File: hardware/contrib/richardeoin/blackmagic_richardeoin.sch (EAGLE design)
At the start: 5 parts, among them Q2 IRLML5103

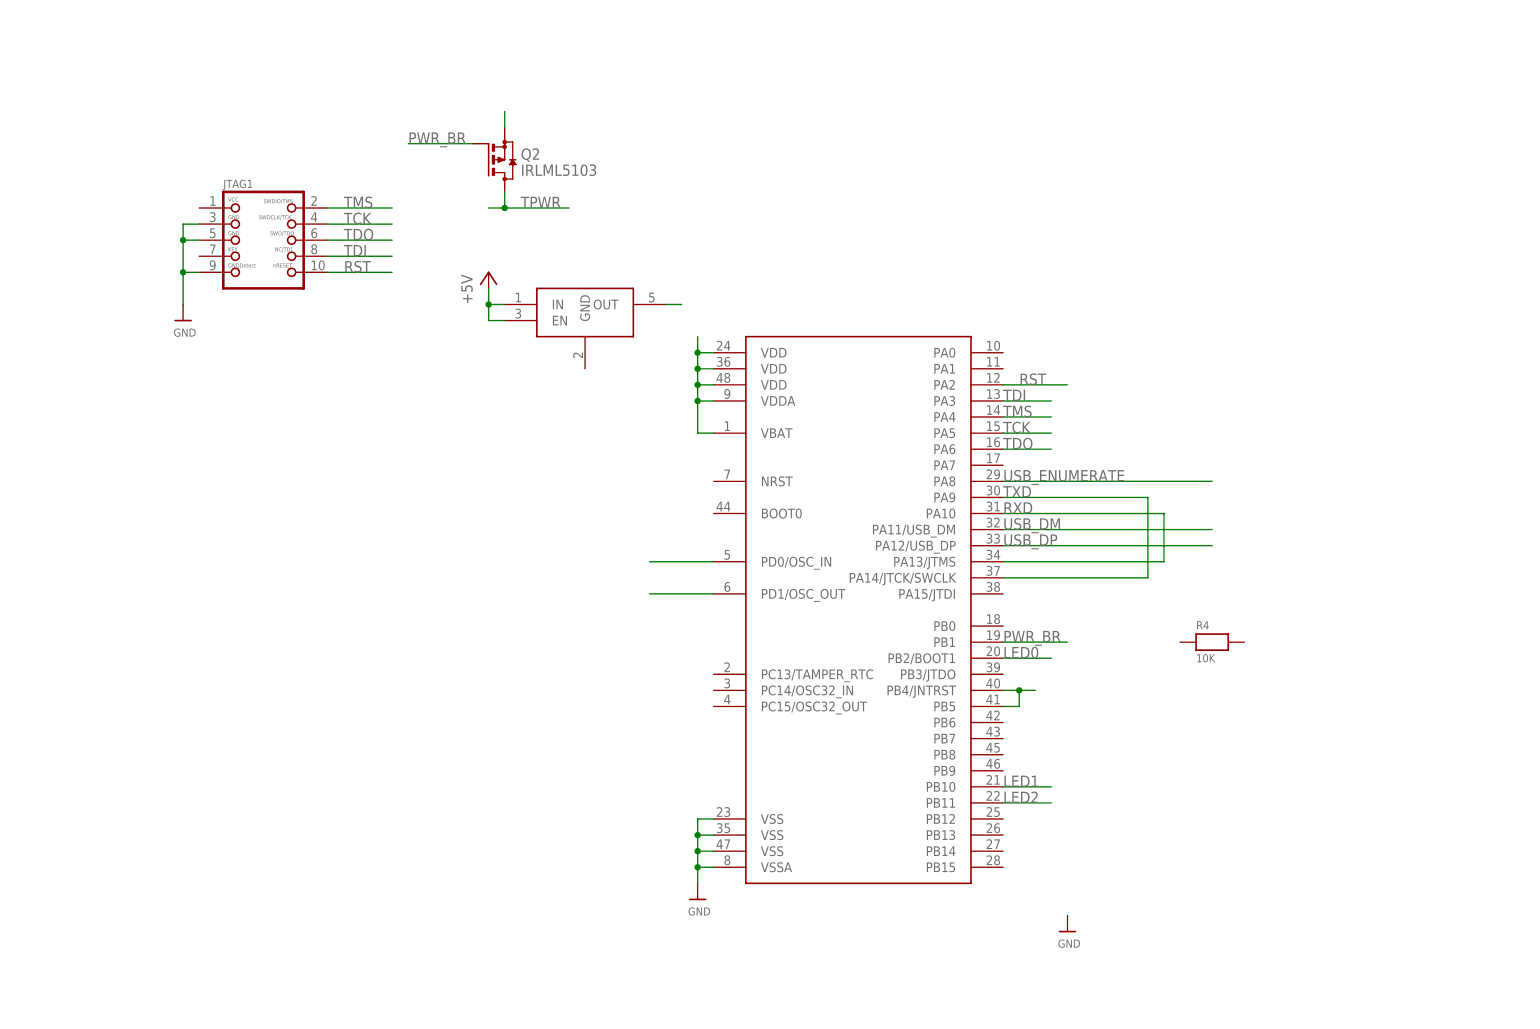
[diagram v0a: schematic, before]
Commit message: Majority of Components in place
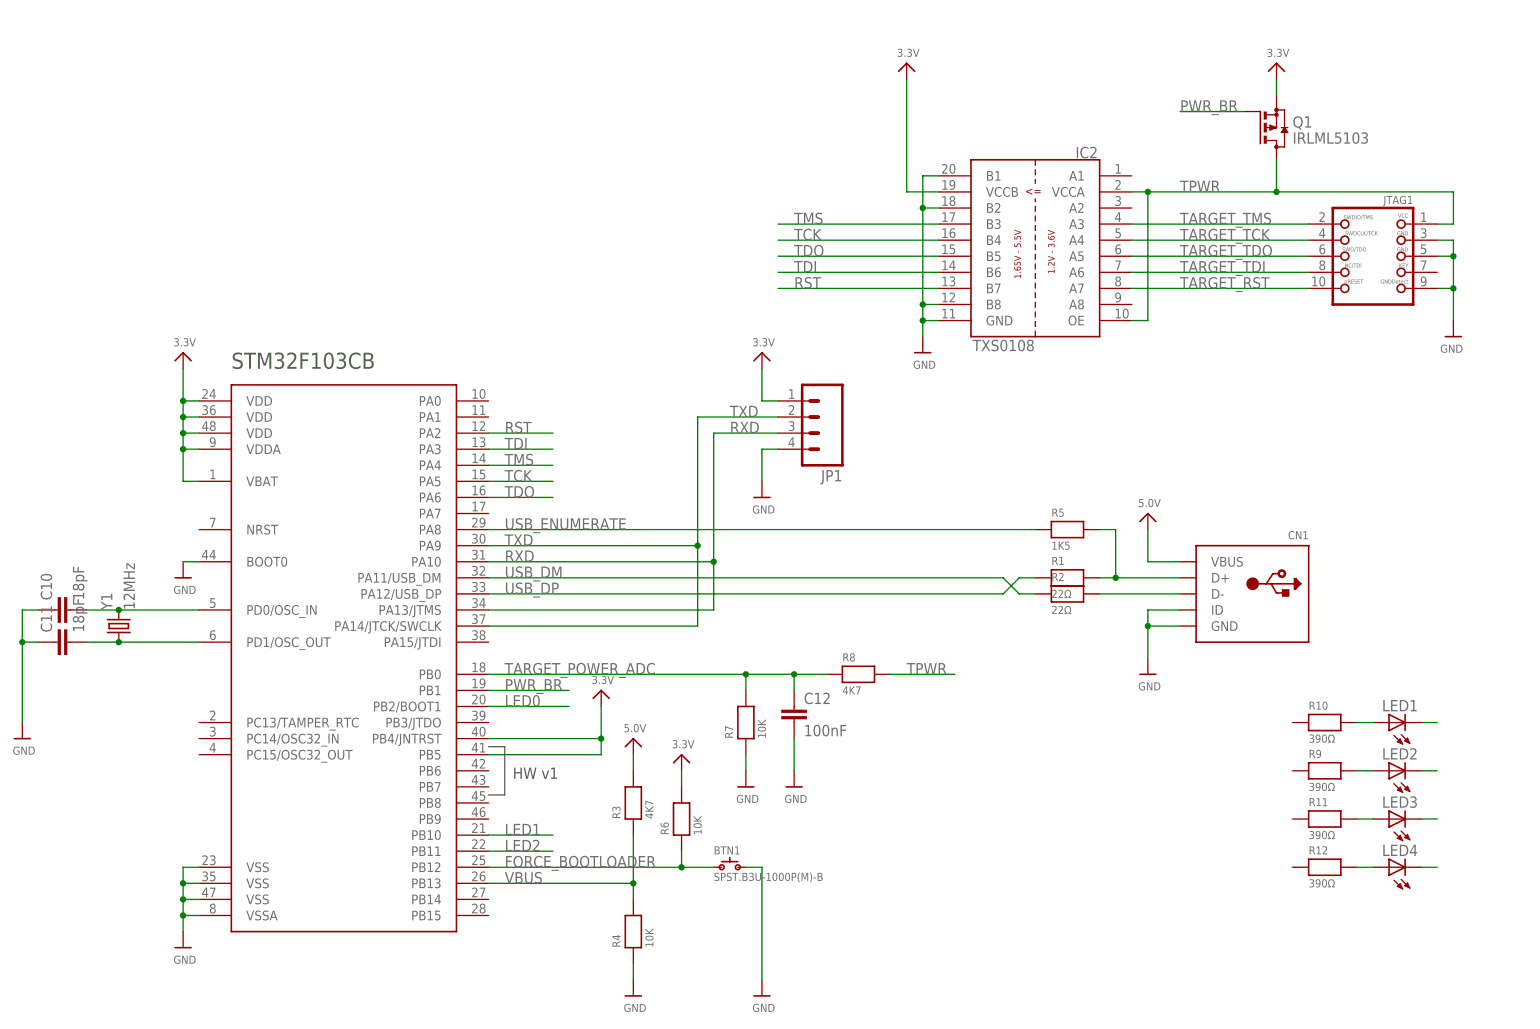
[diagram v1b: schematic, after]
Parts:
- removed Q2: IRLML5103, transistor-small-signal:BSS84
- removed U$1: STM32F_48PIN, stm32f:STM32F_48PIN
- removed U$2: TLV70033DCK, tlv700:TLV700DCK
- added BTN1: SPST.B3U-1000P(M)-B, omron:SPST.B3U-1000P(M)-B
- added C10, C11: 18pF, resistor:C-EUC0603K
- added C12: 100nF, resistor:C-EUC0603K
- added CN1: (no value), microbuilder_v3:USBMINIB
- added IC1: STM32F_48PIN, stm32f:STM32F_48PIN
- added IC2: TXS0108, dan-translate:TX0108PWR
- added JP1: (no value), SparkFun:M04LOCK
- added LED1, LED2, LED3, LED4: (no value), led:LEDCHIPLED_0603
- added Q1: IRLML5103, transistor-small-signal:BSS84
- added R1, R2: 22Ω, microbuilder:RESISTOR0603MINI
- added R10, R11, R12, R9: 390Ω, microbuilder:RESISTOR0603MINI
- added R3, R8: 4K7, microbuilder:RESISTOR0603MINI
- added R5: 1K5, microbuilder:RESISTOR0603MINI
- added R6, R7: 10K, microbuilder:RESISTOR0603MINI
- added Y1: 12MHz, SparkFun:CRYSTAL5X3
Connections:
- removed net +5V: U$2.EN, U$2.IN
- removed net OSC_OUT: U$1.PD1/OSC_OUT
- new net 3.3V: IC1.PB4/JNTRST, IC1.PB5, IC1.VBAT, IC1.VDD@1, IC1.VDD@2, IC1.VDD@3, IC1.VDDA, IC2.VCCB, JP1.1, Q1.S, R6.2
- new net 5.0V: CN1.VBUS, R3.2
- new net D+: CN1.D+, R1.2, R5.2
- new net D-: CN1.D-, R2.2
- new net FORCE_BOOTLOADER: BTN1.1, IC1.PB12, R6.1
- new net LPC_XTAL2: C11.2, IC1.PD1/OSC_OUT, Y1.1
- new net N$3: LED1.C
- new net N$6: LED3.A, R11.2
- new net N$7: LED4.C
- new net N$8: LED4.A, R12.2
- new net TARGET_POWER_ADC: C12.1, IC1.PB0, R7.2, R8.1
- new net TARGET_RST: IC2.A7, JTAG1.10
- new net TARGET_TCK: IC2.A4, JTAG1.4
- new net TARGET_TDI: IC2.A6, JTAG1.8
- new net TARGET_TDO: IC2.A5, JTAG1.6
- new net TARGET_TMS: IC2.A3, JTAG1.2
- new net VBUS: IC1.PB13, R3.1, R4.2
- net GND: now also BTN1.2, C10.1, C11.1, C12.2, CN1.GND, CN1.ID, IC1.BOOT0, IC1.VSS@1, IC1.VSS@2, IC1.VSS@3, IC1.VSSA, IC2.B1, IC2.B2, IC2.B8, IC2.GND, JP1.4, R4.1, R7.1; no longer U$1.VSS@1, U$1.VSS@2, U$1.VSS@3, U$1.VSSA
- net LED0: now also IC1.PB2/BOOT1; no longer U$1.PB2/BOOT1
- net LED1: now also IC1.PB10; no longer U$1.PB10
- net LED2: now also IC1.PB11; no longer U$1.PB11
- net N$1: now also LED2.C; no longer Q2.S
- net N$2: now also LED2.A, R9.2; no longer U$2.OUT
- net N$4: now also LED1.A, R10.2; no longer U$1.VBAT, U$1.VDD@1, U$1.VDD@2, U$1.VDD@3, U$1.VDDA
- net N$5: now also LED3.C; no longer U$1.PB4/JNTRST, U$1.PB5
- net OSC_IN: now also C10.2, IC1.PD0/OSC_IN, Y1.2; no longer U$1.PD0/OSC_IN
- net PWR_BR: now also IC1.PB1, Q1.G; no longer Q2.G, U$1.PB1
- net RST: now also IC1.PA2, IC2.B7; no longer JTAG1.10, U$1.PA2
- net RXD: now also IC1.PA10, IC1.PA13/JTMS, JP1.3; no longer U$1.PA10, U$1.PA13/JTMS
- net TCK: now also IC1.PA5, IC2.B4; no longer JTAG1.4, U$1.PA5
- net TDI: now also IC1.PA3, IC2.B6; no longer JTAG1.8, U$1.PA3
- net TDO: now also IC1.PA6, IC2.B5; no longer JTAG1.6, U$1.PA6
- net TMS: now also IC1.PA4, IC2.B3; no longer JTAG1.2, U$1.PA4
- net TPWR: now also IC2.OE, IC2.VCCA, JTAG1.1, Q1.D, R8.2; no longer Q2.D
- net TXD: now also IC1.PA14/JTCK/SWCLK, IC1.PA9, JP1.2; no longer U$1.PA14/JTCK/SWCLK, U$1.PA9
- net USB_DM: now also IC1.PA11/USB_DM, R2.1; no longer U$1.PA11/USB_DM
- net USB_DP: now also IC1.PA12/USB_DP, R1.1; no longer U$1.PA12/USB_DP
- net USB_ENUMERATE: now also IC1.PA8, R5.1; no longer U$1.PA8
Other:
- note added: "HW v1"
- note added: "STM32F103CB"
- moved on the sheet: JTAG1, R4

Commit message: Added LEDs
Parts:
- removed LED1, LED2, LED4: (no value), led:LEDCHIPLED_0603
- added D1: GREEN, led:LEDCHIPLED_0603
- added D2: RED, led:LEDCHIPLED_0603
- added D3: YELLOW, led:LEDCHIPLED_0603
- D4: value (none) -> YELLOW
- Y1: value 12MHz -> 8MHz
- renumbered LED3 to D4
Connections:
- removed net N$1: LED2.C
- removed net N$3: LED1.C
- removed net N$5: D4.C
- removed net N$7: LED4.C
- net 3.3V: now also R10.1
- net GND: now also D1.C, D2.C, D3.C, D4.C
- net LED0: now also R12.1
- net LED1: now also R11.1
- net LED2: now also R9.1
- net N$2: now also D2.A; no longer LED2.A
- net N$4: now also D1.A; no longer LED1.A
- net N$6: now also D3.A; no longer D4.A
- net N$8: now also D4.A; no longer LED4.A
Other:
- moved on the sheet: BTN1, C10, C11, C12, CN1, IC2, JP1, JTAG1, Q1, R1, R10, R11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

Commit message: Schematic provisionally complete
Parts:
- added C1, C2: 1µF, resistor:C-EUC0603K
- added C3, C4, C5: 100nF, resistor:C-EUC0603K
- added U$21: TLV70033DCK, tlv700:TLV700DCK
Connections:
- net 3.3V: now also C2.1, C3.1, C4.1, C5.1, U$21.OUT
- net 5.0V: now also C1.1, U$21.EN, U$21.IN
- net GND: now also C1.2, C2.2, C3.2, C4.2, C5.2, U$21.GND
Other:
- note added: "TLV70033"
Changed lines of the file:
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@@
 <part name="U$19" library="microbuilder_v3" deviceset="GND" device=""/>
 <part name="U$20" library="microbuilder_v3" deviceset="3.3V" device=""/>
+<part name="U$21" library="tlv700" deviceset="TLV700" device="DCK" value="TLV70033DCK"/>
+<part name="U$22" library="microbuilder" deviceset="GND" device=""/>
+<part name="C1" library="resistor" deviceset="C-EU" device="C0603K" value="1µF"/>
+<part name="U$23" library="microbuilder_v3" deviceset="5.0V" device=""/>
+<part name="C2" library="resistor" deviceset="C-EU" device="C0603K" value="1µF"/>
+<part name="U$24" library="microbuilder" deviceset="GND" device=""/>
+<part name="C3" library="resistor" deviceset="C-EU" device="C0603K" value="100nF"/>
+<part name="C4" library="resistor" deviceset="C-EU" device="C0603K" value="100nF"/>
+<part name="C5" library="resistor" deviceset="C-EU" device="C0603K" value="100nF"/>
+<part name="U$25" library="microbuilder" deviceset="GND" device=""/>
+<part name="U$26" library="microbuilder" deviceset="GND" device=""/>
+<part name="U$27" library="microbuilder" deviceset="GND" device=""/>
+<part name="U$28" library="microbuilder" deviceset="GND" device=""/>
+<part name="U$31" library="microbuilder_v3" deviceset="3.3V" device=""/>
 </parts>
 <sheets>
@@
 <wire x1="81.28" y1="77.47" x2="81.28" y2="69.85" width="0.1524" layer="97"/>
 <wire x1="81.28" y1="69.85" x2="78.74" y2="69.85" width="0.1524" layer="97"/>
+<text x="30.48" y="175.26" size="1.778" layer="97" font="vector" ratio="12">TLV70033</text>
 </plain>
 <instances>
@@
 <instance part="U$19" gate="G$1" x="231.14" y="40.64"/>
 <instance part="U$20" gate="G$1" x="200.66" y="88.9"/>
+<instance part="U$21" gate="G$1" x="30.48" y="165.1"/>
+<instance part="U$22" gate="G$1" x="38.1" y="154.94"/>
+<instance part="C1" gate="G$1" x="17.78" y="165.1"/>
+<instance part="U$23" gate="G$1" x="17.78" y="177.8"/>
+<instance part="C2" gate="G$1" x="55.88" y="165.1"/>
+<instance part="U$24" gate="G$1" x="17.78" y="154.94"/>
+<instance part="C3" gate="G$1" x="66.04" y="165.1"/>
+<instance part="C4" gate="G$1" x="76.2" y="165.1"/>
+<instance part="C5" gate="G$1" x="86.36" y="165.1"/>
+<instance part="U$25" gate="G$1" x="55.88" y="154.94"/>
+<instance part="U$26" gate="G$1" x="66.04" y="154.94"/>
+<instance part="U$27" gate="G$1" x="76.2" y="154.94"/>
+<instance part="U$28" gate="G$1" x="86.36" y="154.94"/>
+<instance part="U$31" gate="G$1" x="86.36" y="177.8"/>
 </instances>
 <busses>
@@
 <junction x="231.14" y="63.5"/>
 <junction x="231.14" y="53.34"/>
+</segment>
+<segment>
+<pinref part="C1" gate="G$1" pin="2"/>
+<pinref part="U$24" gate="G$1" pin="GND"/>
+<wire x1="17.78" y1="160.02" x2="17.78" y2="157.48" width="0.1524" layer="91"/>
+</segment>
+<segment>
+<pinref part="U$22" gate="G$1" pin="GND"/>
+<pinref part="U$21" gate="G$1" pin="GND"/>
+<wire x1="38.1" y1="157.48" x2="38.1" y2="160.02" width="0.1524" layer="91"/>
+</segment>
+<segment>
+<pinref part="U$28" gate="G$1" pin="GND"/>
+<pinref part="C5" gate="G$1" pin="2"/>
+<wire x1="86.36" y1="157.48" x2="86.36" y2="160.02" width="0.1524" layer="91"/>
+</segment>
+<segment>
+<pinref part="U$27" gate="G$1" pin="GND"/>
+<pinref part="C4" gate="G$1" pin="2"/>
+<wire x1="76.2" y1="157.48" x2="76.2" y2="160.02" width="0.1524" layer="91"/>
+</segment>
+<segment>
+<pinref part="U$26" gate="G$1" pin="GND"/>
+<pinref part="C3" gate="G$1" pin="2"/>
+<wire x1="66.04" y1="157.48" x2="66.04" y2="160.02" width="0.1524" layer="91"/>
+</segment>
+<segment>
+<pinref part="U$25" gate="G$1" pin="GND"/>
+<pinref part="C2" gate="G$1" pin="2"/>
+<wire x1="55.88" y1="157.48" x2="55.88" y2="160.02" width="0.1524" layer="91"/>
 </segment>
 </net>
@@
 <wire x1="200.66" y1="83.82" x2="200.66" y2="86.36" width="0.1524" layer="91"/>
 </segment>
+<segment>
+<pinref part="U$21" gate="G$1" pin="OUT"/>
+<pinref part="C2" gate="G$1" pin="1"/>
+<wire x1="50.8" y1="170.18" x2="55.88" y2="170.18" width="0.1524" layer="91"/>
+<wire x1="55.88" y1="170.18" x2="55.88" y2="167.64" width="0.1524" layer="91"/>
+<pinref part="C3" gate="G$1" pin="1"/>
+<wire x1="55.88" y1="170.18" x2="66.04" y2="170.18" width="0.1524" layer="91"/>
+<wire x1="66.04" y1="170.18" x2="66.04" y2="167.64" width="0.1524" layer="91"/>
+<pinref part="C4" gate="G$1" pin="1"/>
+<wire x1="66.04" y1="170.18" x2="76.2" y2="170.18" width="0.1524" layer="91"/>
+<wire x1="76.2" y1="170.18" x2="76.2" y2="167.64" width="0.1524" layer="91"/>
+<pinref part="C5" gate="G$1" pin="1"/>
+<wire x1="76.2" y1="170.18" x2="86.36" y2="170.18" width="0.1524" layer="91"/>
+<wire x1="86.36" y1="170.18" x2="86.36" y2="167.64" width="0.1524" layer="91"/>
+<junction x="55.88" y="170.18"/>
+<junction x="66.04" y="170.18"/>
+<junction x="76.2" y="170.18"/>
+<junction x="86.36" y="170.18"/>
+<pinref part="U$31" gate="G$1" pin="3.3V"/>
+<wire x1="86.36" y1="170.18" x2="86.36" y2="175.26" width="0.1524" layer="91"/>
+</segment>
 </net>
 <net name="D+" class="0">
@@
 <wire x1="101.6" y1="76.2" x2="101.6" y2="73.66" width="0.1524" layer="91"/>
 </segment>
-</net>
+<segment>
+<pinref part="U$23" gate="G$1" pin="5.0V"/>
+<pinref part="C1" gate="G$1" pin="1"/>
+<wire x1="17.78" y1="175.26" x2="17.78" y2="170.18" width="0.1524" layer="91"/>
+<pinref part="U$21" gate="G$1" pin="IN"/>
+<wire x1="17.78" y1="170.18" x2="17.78" y2="167.64" width="0.1524" layer="91"/>
+<wire x1="25.4" y1="170.18" x2="22.86" y2="170.18" width="0.1524" layer="91"/>
+<wire x1="22.86" y1="170.18" x2="22.86" y2="167.64" width="0.1524" layer="91"/>
+<pinref part="U$21" gate="G$1" pin="EN"/>
+<wire x1="22.86" y1="167.64" x2="25.4" y2="167.64" width="0.1524" layer="91"/>
+<wire x1="22.86" y1="170.18" x2="17.78" y2="170.18" width="0.1524" layer="91"/>
+<junction x="22.86" y="170.18"/>
+<junction x="17.78" y="170.18"/>
+</segment>
+</net>

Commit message: Completed board layout
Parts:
- renumbered U$21 to IC3
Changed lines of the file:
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@@
 <part name="U$19" library="microbuilder_v3" deviceset="GND" device=""/>
 <part name="U$20" library="microbuilder_v3" deviceset="3.3V" device=""/>
-<part name="U$21" library="tlv700" deviceset="TLV700" device="DCK" value="TLV70033DCK"/>
+<part name="IC3" library="tlv700" deviceset="TLV700" device="DCK" value="TLV70033DCK"/>
 <part name="U$22" library="microbuilder" deviceset="GND" device=""/>
 <part name="C1" library="resistor" deviceset="C-EU" device="C0603K" value="1µF"/>
@@
 <instance part="U$19" gate="G$1" x="231.14" y="40.64"/>
 <instance part="U$20" gate="G$1" x="200.66" y="88.9"/>
-<instance part="U$21" gate="G$1" x="30.48" y="165.1"/>
+<instance part="IC3" gate="G$1" x="30.48" y="165.1"/>
 <instance part="U$22" gate="G$1" x="38.1" y="154.94"/>
 <instance part="C1" gate="G$1" x="17.78" y="165.1"/>
@@
 <segment>
 <pinref part="U$22" gate="G$1" pin="GND"/>
-<pinref part="U$21" gate="G$1" pin="GND"/>
+<pinref part="IC3" gate="G$1" pin="GND"/>
 <wire x1="38.1" y1="157.48" x2="38.1" y2="160.02" width="0.1524" layer="91"/>
 </segment>
@@
 </segment>
 <segment>
-<pinref part="U$21" gate="G$1" pin="OUT"/>
+<pinref part="IC3" gate="G$1" pin="OUT"/>
 <pinref part="C2" gate="G$1" pin="1"/>
 <wire x1="50.8" y1="170.18" x2="55.88" y2="170.18" width="0.1524" layer="91"/>
@@
 <pinref part="C1" gate="G$1" pin="1"/>
 <wire x1="17.78" y1="175.26" x2="17.78" y2="170.18" width="0.1524" layer="91"/>
-<pinref part="U$21" gate="G$1" pin="IN"/>
+<pinref part="IC3" gate="G$1" pin="IN"/>
 <wire x1="17.78" y1="170.18" x2="17.78" y2="167.64" width="0.1524" layer="91"/>
 <wire x1="25.4" y1="170.18" x2="22.86" y2="170.18" width="0.1524" layer="91"/>
-<wire x1="22.86" y1="170.18" x2="22.86" y2="167.64" width="0.1524" layer="91"/>
-<pinref part="U$21" gate="G$1" pin="EN"/>
+<junction x="17.78" y="170.18"/>
+<pinref part="IC3" gate="G$1" pin="EN"/>
+<wire x1="22.86" y1="170.18" x2="17.78" y2="170.18" width="0.1524" layer="91"/>
 <wire x1="22.86" y1="167.64" x2="25.4" y2="167.64" width="0.1524" layer="91"/>
-<wire x1="22.86" y1="170.18" x2="17.78" y2="170.18" width="0.1524" layer="91"/>
+<wire x1="22.86" y1="167.64" x2="22.86" y2="170.18" width="0.1524" layer="91"/>
 <junction x="22.86" y="170.18"/>
-<junction x="17.78" y="170.18"/>
-</segment>
-</net>
+</segment>
+</net>

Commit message: Changed text on the end of the board to "ARM Cortex Debug"
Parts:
- R3: value 4K7 -> 1K5
- R5: value 1K5 -> 10K
- R7: value 10K -> 4K7
- renumbered C10 to C7, C11 to C8, C12 to C6
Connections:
- net 3.3V: now also R5.2, R9.1; no longer R10.1, R6.2
- net 5.0V: now also R7.2; no longer R3.2
- net D+: now also R3.2; no longer R5.2
- net FORCE_BOOTLOADER: now also R5.1; no longer R6.1
- net GND: now also R6.1; no longer R7.1
- net LED2: now also R10.1; no longer R9.1
- net N$2: now also R10.2; no longer R9.2
- net N$4: now also R9.2; no longer R10.2
- net TARGET_POWER_ADC: now also R6.2; no longer R7.2
- net USB_ENUMERATE: now also R3.1; no longer R5.1
- net VBUS: now also R7.1; no longer R3.1
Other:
- moved on the sheet: R10, R3, R5, R6, R7, R9

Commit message: Added switch on BOOT0
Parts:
- added BTN2: SPST.B3U-1000P(M)-B, omron:SPST.B3U-1000P(M)-B
- added R13: 10K, microbuilder:RESISTOR0603MINI
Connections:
- new net BOOT0: BTN2.1, IC1.BOOT0, R13.2
- net 3.3V: now also BTN2.2
- net GND: now also R13.1; no longer IC1.BOOT0
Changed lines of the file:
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@@
 <part name="R4" library="microbuilder" deviceset="RESISTOR" device="0603MINI" value="10K"/>
 <part name="U$3" library="microbuilder_v3" deviceset="3.3V" device=""/>
-<part name="U$2" library="microbuilder_v3" deviceset="GND" device=""/>
 <part name="CN1" library="microbuilder_v3" deviceset="USB" device="MINIB"/>
 <part name="R1" library="microbuilder" deviceset="RESISTOR" device="0603MINI" value="22Ω"/>
@@
 <part name="U$28" library="microbuilder" deviceset="GND" device=""/>
 <part name="U$31" library="microbuilder_v3" deviceset="3.3V" device=""/>
+<part name="BTN2" library="omron" deviceset="SPST" device=".B3U-1000P(M)-B"/>
+<part name="R13" library="microbuilder" deviceset="RESISTOR" device="0603MINI" value="10K"/>
+<part name="U$2" library="microbuilder_v3" deviceset="3.3V" device=""/>
 </parts>
 <sheets>
@@
 <instance part="R4" gate="G$1" x="101.6" y="48.26" rot="R90"/>
 <instance part="U$3" gate="G$1" x="30.48" y="139.7"/>
-<instance part="U$2" gate="G$1" x="30.48" y="104.14"/>
 <instance part="CN1" gate="G$1" x="198.12" y="101.6" rot="MR0"/>
 <instance part="R1" gate="G$1" x="170.18" y="104.14"/>
@@
 <instance part="U$28" gate="G$1" x="86.36" y="154.94"/>
 <instance part="U$31" gate="G$1" x="86.36" y="177.8"/>
+<instance part="BTN2" gate="G$1" x="20.32" y="119.38" rot="R90"/>
+<instance part="R13" gate="G$1" x="12.7" y="106.68"/>
+<instance part="U$2" gate="G$1" x="20.32" y="139.7"/>
 </instances>
 <busses>
@@
 </segment>
 <segment>
-<pinref part="IC1" gate="G$1" pin="BOOT0"/>
-<pinref part="U$2" gate="G$1" pin="GND"/>
-<wire x1="33.02" y1="106.68" x2="30.48" y2="106.68" width="0.1524" layer="91"/>
-</segment>
-<segment>
 <pinref part="CN1" gate="G$1" pin="ID"/>
 <pinref part="U$5" gate="G$1" pin="GND"/>
@@
 <pinref part="C8" gate="G$1" pin="1"/>
 <pinref part="U$16" gate="G$1" pin="GND"/>
+<pinref part="R13" gate="G$1" pin="1"/>
+<wire x1="7.62" y1="106.68" x2="5.08" y2="106.68" width="0.1524" layer="91"/>
+<wire x1="5.08" y1="106.68" x2="5.08" y2="99.06" width="0.1524" layer="91"/>
+<junction x="5.08" y="99.06"/>
 </segment>
 <segment>
@@
 <wire x1="86.36" y1="170.18" x2="86.36" y2="175.26" width="0.1524" layer="91"/>
 </segment>
+<segment>
+<pinref part="U$2" gate="G$1" pin="3.3V"/>
+<pinref part="BTN2" gate="G$1" pin="2"/>
+<wire x1="20.32" y1="137.16" x2="20.32" y2="121.92" width="0.1524" layer="91"/>
+</segment>
 </net>
 <net name="D+" class="0">
@@
 </segment>
 </net>
+<net name="BOOT0" class="0">
+<segment>
+<pinref part="IC1" gate="G$1" pin="BOOT0"/>
+<pinref part="R13" gate="G$1" pin="2"/>
+<wire x1="17.78" y1="106.68" x2="20.32" y2="106.68" width="0.1524" layer="91"/>
+<pinref part="BTN2" gate="G$1" pin="1"/>
+<wire x1="20.32" y1="106.68" x2="33.02" y2="106.68" width="0.1524" layer="91"/>
+<wire x1="20.32" y1="116.84" x2="20.32" y2="106.68" width="0.1524" layer="91"/>
+<junction x="20.32" y="106.68"/>
+</segment>
+</net>
